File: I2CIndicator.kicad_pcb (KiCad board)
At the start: 2 copper layers, 19 parts, among them Q1 BS107, Q2 BS107, Q3 BS107, U1 PCA9685

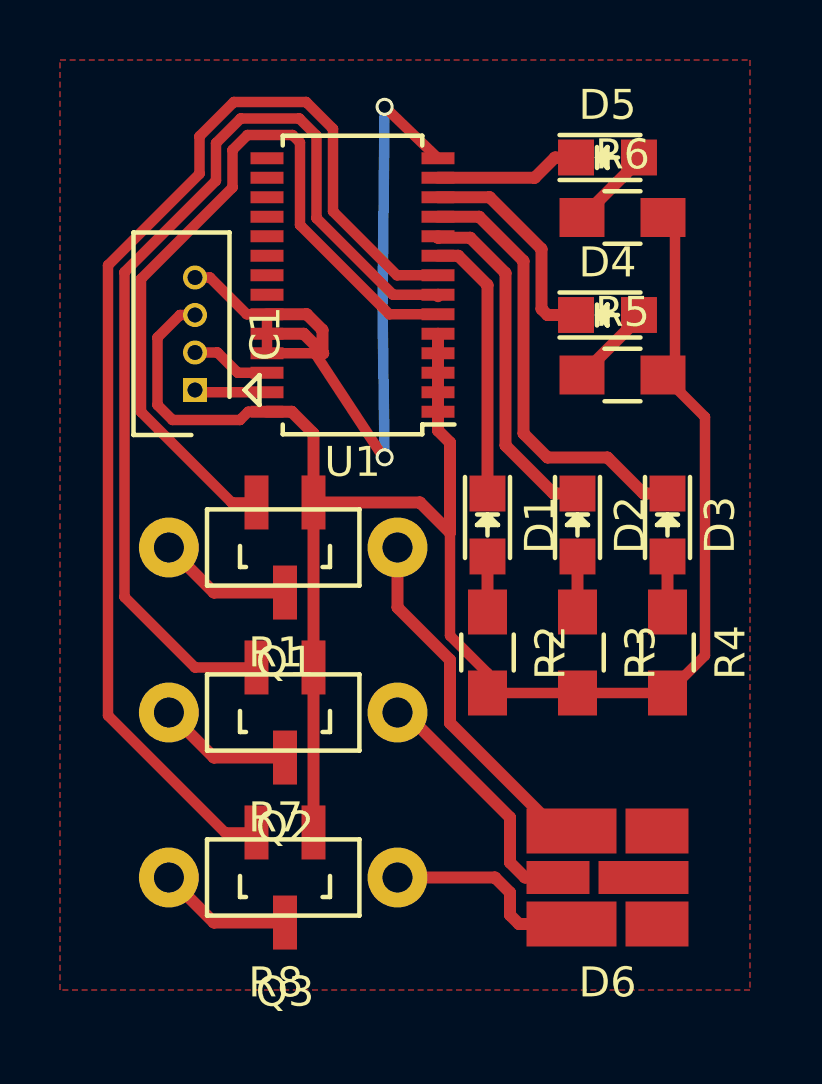
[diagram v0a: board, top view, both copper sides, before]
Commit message: Modified to use SunLED XZCB25MO24DG25X111S
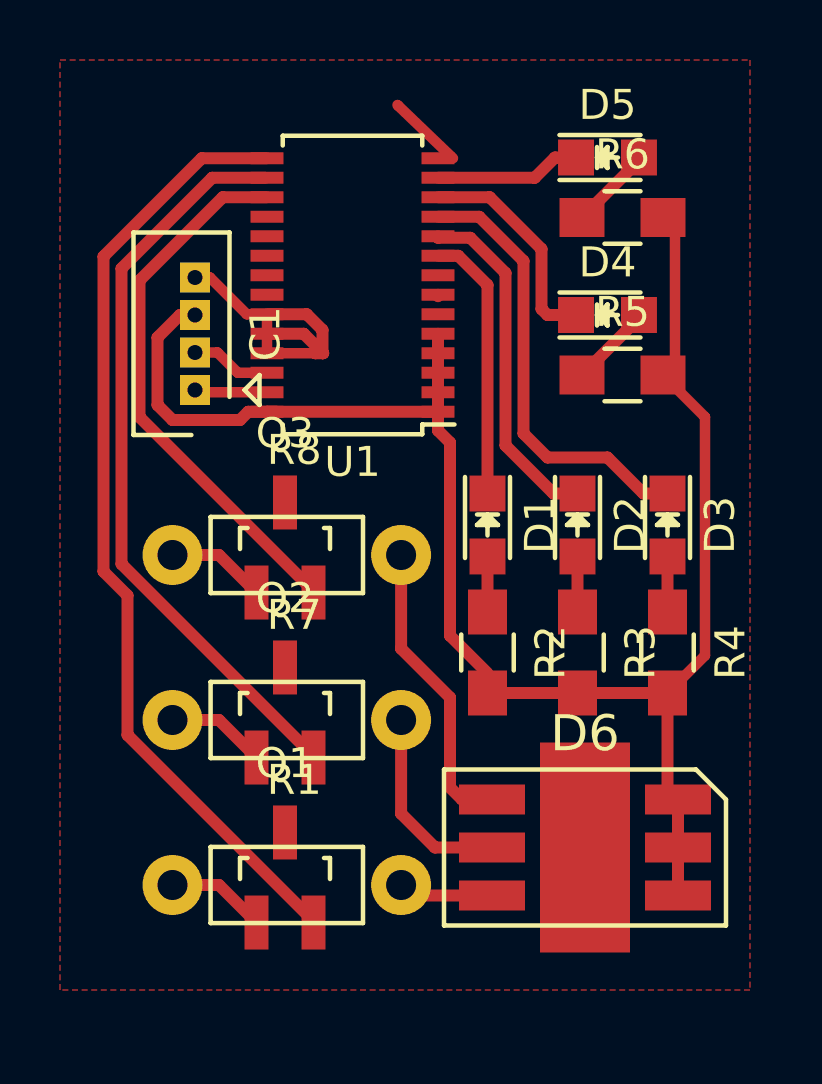
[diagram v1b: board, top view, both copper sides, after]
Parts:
- D6: value LED_RGB -> LED_BRG_EP; footprint LEDs:LED_RGB_PLLC-6_HandSoldering -> LEDs:SunLED-XZ
- moved R1 13.5 mm to (140.2, 125.0), turned to 0 degrees
- moved R8 13.1 mm to (140.2, 114.0), turned to 0 degrees
- moved Q1 11.0 mm to (144.0, 124.8), turned to 0 degrees
- moved Q3 11.0 mm to (144.0, 113.8), turned to 0 degrees
- moved R7 7.50 mm to (140.2, 119.5), turned to 0 degrees
- moved D6 1.25 mm to (154.0, 123.8), turned to 270 degrees
- turned Q2 to 0 degrees
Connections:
- D6 pad 1: GND -> Net-(D6-Pad1)
- D6 pad 2: GND -> Net-(D6-Pad2)
- D6 pad 3: GND -> Net-(D6-Pad3)
- D6 pad 4: Net-(D6-Pad4) -> +5V
- D6 pad 5: Net-(D6-Pad5) -> +5V
- D6 pad 6: Net-(D6-Pad6) -> +5V
- Q1 pad 1: +5V -> Net-(Q1-Pad1)
- Q1 pad 3: Net-(Q1-Pad3) -> GND
- Q2 pad 1: +5V -> Net-(Q2-Pad1)
- Q2 pad 3: Net-(Q2-Pad3) -> GND
- Q3 pad 1: +5V -> Net-(Q3-Pad1)
- Q3 pad 3: Net-(Q3-Pad3) -> GND
- R1 pad 1: Net-(D6-Pad4) -> Net-(Q1-Pad1)
- R1 pad 2: Net-(Q1-Pad3) -> Net-(D6-Pad3)
- R7 pad 1: Net-(D6-Pad5) -> Net-(Q2-Pad1)
- R7 pad 2: Net-(Q2-Pad3) -> Net-(D6-Pad2)
- R8 pad 1: Net-(D6-Pad6) -> Net-(Q3-Pad1)
- R8 pad 2: Net-(Q3-Pad3) -> Net-(D6-Pad1)
- U1 pad 15: (no net) -> Net-(Q1-Pad2)
- U1 pad 16: (no net) -> Net-(Q2-Pad2)
- U1 pad 17: (no net) -> Net-(Q3-Pad2)
- U1 pad 18: (no net) -> Net-(U1-Pad18)
- U1 pad 19: (no net) -> Net-(U1-Pad19)
- U1 pad 20: (no net) -> Net-(U1-Pad20)
- U1 pad 21: (no net) -> Net-(U1-Pad21)
- U1 pad 22: (no net) -> Net-(U1-Pad22)
- U1 pad 6: Net-(Q1-Pad2) -> Net-(U1-Pad6)
- U1 pad 7: Net-(Q2-Pad2) -> Net-(U1-Pad7)
- U1 pad 8: Net-(Q3-Pad2) -> Net-(U1-Pad8)
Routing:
- net Net-(Q3-Pad2): track 39.9 -> 18.2 mm
- net GND: track 29.5 -> 13.7 mm, vias 2 -> 0
- net Net-(D6-Pad4): track 11.7 -> 0.00 mm
- net Net-(D6-Pad1): track 0.00 -> 9.99 mm
- net Net-(D6-Pad5): track 8.96 -> 0.00 mm
- net Net-(Q2-Pad2): track 33.6 -> 25.1 mm
- net +5V: track 63.9 -> 56.7 mm
- net Net-(D6-Pad2): track 0.00 -> 6.62 mm
- net Net-(D6-Pad6): track 6.43 -> 0.00 mm
- net Net-(Q1-Pad2): track 26.2 -> 31.9 mm
- net Net-(Q3-Pad3): track 4.49 -> 0.00 mm
- net Net-(Q2-Pad3): track 4.49 -> 0.00 mm
- net Net-(Q1-Pad3): track 4.49 -> 0.00 mm
- net Net-(Q3-Pad1): track 0.00 -> 3.32 mm
- net Net-(Q2-Pad1): track 0.00 -> 3.32 mm
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
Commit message: Found wrong component was used for N-MOSFET transistors resulting in wrong layout. Fixed schamatic, but layout needs to be fixed.
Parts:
- Q1, Q2, Q3: value BS107 -> BSS138
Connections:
- Q1 pad 2: Net-(Q1-Pad2) -> GND
- Q1 pad 3: GND -> Net-(Q1-Pad3)
- Q2 pad 2: Net-(Q2-Pad2) -> GND
- Q2 pad 3: GND -> Net-(Q2-Pad3)
- Q3 pad 2: Net-(Q3-Pad2) -> GND
- Q3 pad 3: GND -> Net-(Q3-Pad3)
- R1 pad 1: Net-(Q1-Pad1) -> Net-(Q1-Pad3)
- R7 pad 1: Net-(Q2-Pad1) -> Net-(Q2-Pad3)
- R8 pad 1: Net-(Q3-Pad1) -> Net-(Q3-Pad3)
- U1 pad 15: Net-(Q1-Pad2) -> Net-(Q1-Pad1)
- U1 pad 16: Net-(Q2-Pad2) -> Net-(Q2-Pad1)
- U1 pad 17: Net-(Q3-Pad2) -> Net-(Q3-Pad1)
- U1 pad 18: Net-(U1-Pad18) -> (no net)
- U1 pad 19: Net-(U1-Pad19) -> (no net)
- U1 pad 20: Net-(U1-Pad20) -> (no net)
- U1 pad 21: Net-(U1-Pad21) -> (no net)
- U1 pad 22: Net-(U1-Pad22) -> (no net)
- U1 pad 6: Net-(U1-Pad6) -> (no net)
- U1 pad 7: Net-(U1-Pad7) -> (no net)
- U1 pad 8: Net-(U1-Pad8) -> (no net)
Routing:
- net GND: track 13.7 -> 75.3 mm
- net Net-(Q1-Pad2): track 31.9 -> 0.00 mm
- net Net-(Q2-Pad2): track 25.1 -> 0.00 mm
- net Net-(Q3-Pad2): track 18.2 -> 0.00 mm
- net Net-(Q2-Pad1): track 3.32 -> 7.82 mm
- net Net-(Q3-Pad1): track 3.32 -> 7.17 mm
- net Net-(Q3-Pad3): track 0.00 -> 1.55 mm
- net Net-(Q2-Pad3): track 0.00 -> 1.55 mm
- net Net-(Q1-Pad3): track 0.00 -> 1.55 mm
- net Net-(Q1-Pad1): track 3.32 -> 3.94 mm

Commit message: Fixed the layout
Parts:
- moved Q1 1.35 mm to (142.8, 125.2), turned to 135 degrees
- moved Q2 1.35 mm to (142.8, 119.8), turned to 135 degrees
- moved Q3 1.35 mm to (142.8, 114.2), turned to 135 degrees
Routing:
- net GND: track 75.3 -> 13.7 mm
- net Net-(Q1-Pad1): track 3.94 -> 31.6 mm
- net Net-(Q2-Pad1): track 7.82 -> 24.7 mm
- net Net-(Q3-Pad1): track 7.17 -> 17.9 mm
